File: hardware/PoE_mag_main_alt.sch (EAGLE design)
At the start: 100 parts, among them IC1 LD1117S33TR, IC2 DS1338, IC3 74LVC1T45SOT23-HAND, IC4 ATMEGA1284, IC5 MCP2200, IC6 TSR 1-2450, IC7 74LVC1T45SOT23-HAND, IC8 74LVC1T45SOT23-HAND, IC9 74LVC1T45SOT23-HAND, Q1 2N7002, X1 PWR, X2 JTAG, X3 USB, X4 CONN-SMATHD, X5 UFL, X6 MICRO-SD-SOCKETHIROSE-DM3D, Y1 32k768, Y2 16MHz, Y3 12MHz

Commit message: Layout fixes
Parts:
- added C32: 4u7, SteveMarple:CAP_POLPTH2
- added C33, C34, C35, C36: 100n, SteveMarple:C-EU1206-HAND
- renumbered U$16 to U$2, U$18 to U$3, U$19 to U$4, U$20 to U$5, U$21 to U$6, U$22 to U$7, U$23 to U$8, U$24 to U$9, U$25 to U$10
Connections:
- net +3V3: now also C30.1, C35.1, C36.1; no longer C31.1
- net +5V: no longer C30.1
- net GND: now also C32.-, C33.2, C34.2, C35.2, C36.2
- net VCC: now also C33.1, C34.1
- net V_ANT: now also C31.1, C32.+
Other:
- note added: "74LVC1T45 decoupling"
- note removed: "Battery backup"
- moved on the sheet: C23, C24, C25, C26, C30, C31, JP6

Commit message: Add magnetometer level shifting
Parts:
- added C37, C38: 100n, SteveMarple:C-EU1206-HAND
- added D3: BAS40, SteveMarple:DIODE-SCHOTTKYSOT23-1-3-HAND
- added IC10: PCA9517A, SteveMarple:PCA9517ASOIC
- added JP12: 5V LINK, SparkFun:JUMPER-2PTH
- added JP13: MAG VCC, SparkFun:JUMPER-3PTH
- added R14, R15, R16, R17: 10k, SteveMarple:RESISTOR1206-HAND
- added R18: 3k, SteveMarple:RESISTOR1206-HAND
- added R19: 1k, SteveMarple:RESISTOR1206-HAND
- added X7: RJ45, SteveMarple:RJ45-8PTH
- added X8: RJ11, SteveMarple:RJ11-6PTH
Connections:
- new net MAG_SCL: IC10.SCL_B, R17.1, X7.5, X8.4
- new net MAG_SDA: IC10.SDA_B, R16.1, X7.7, X8.6
- new net MAG_VCC: C37.1, IC10.EN, IC10.VCC_B, JP12.2, R16.2, R17.2, X7.6, X8.5
- new net N$26: JP13.2, X7.8
- net +3V3: now also JP13.3
- net +5V: now also JP12.1
- net 20(SDA): now also IC10.SDA_A, R15.1
- net 21(SCL): now also IC10.SCL_A, R14.1
- net A2: now also D3.A, R18.2, R19.2
- net GND: now also C37.2, C38.2, IC10.GND, R19.1, X7.3, X7.4, X8.2, X8.3
- net VCC: now also C38.1, D3.C, IC10.VCC_A, R14.2, R15.2
- net VIN: now also JP13.1, R18.1, X7.2, X8.1
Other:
- note added: "2.1"
- note added: "SHUTDOWN held low permanently for PoE operation"
- note added: "Voltage selection for battery or power-over-ethernet operation."

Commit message: Add schematics and boards for various modules
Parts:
- added D4: BAS21, SteveMarple:DIODESOT23-1-3-HAND
- added Q2: BSS138, SteveMarple:BSS138SOT23-3-HAND
- added R20: 1M, SteveMarple:RESISTOR1206-HAND
- added R21: 330R, SteveMarple:RESISTOR1206-HAND
- added X9: 22-23-2021, con-molex:22-23-2021
- Q1: value 2N7002 -> BSS138; device SteveMarple:2N7002 -> SteveMarple:BSS138SOT23-3-HAND
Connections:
- new net N$27: D4.C, Q2.D, X9-2.S
- new net N$29: Q2.G, R20.2, R21.2
- net 8: now also R21.1
- net GND: now also D4.A, Q2.S, R20.1
- net VIN: now also X9-1.S
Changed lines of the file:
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@@
 <part name="FRAME1" library="SteveMarple" deviceset="FRAME-A3" device=""/>
 <part name="X3" library="SteveMarple" deviceset="USB" device="PTH" value="USB"/>
-<part name="Q1" library="SteveMarple" deviceset="2N7002" device=""/>
+<part name="Q1" library="SteveMarple" deviceset="BSS138" device="SOT23-3-HAND" value="BSS138"/>
 <part name="IC2" library="SteveMarple" deviceset="DS1307" device="SO08" value="DS1338"/>
 <part name="LED1" library="SparkFun" deviceset="LED" device="3MM" value="D13"/>
@@
 <part name="GND45" library="supply1" deviceset="GND" device=""/>
 <part name="GND46" library="supply1" deviceset="GND" device=""/>
+<part name="R20" library="SteveMarple" deviceset="RESISTOR" device="1206-HAND" value="1M"/>
+<part name="R21" library="SteveMarple" deviceset="RESISTOR" device="1206-HAND" value="330R"/>
+<part name="GND47" library="supply1" deviceset="GND" device=""/>
+<part name="Q2" library="SteveMarple" deviceset="BSS138" device="SOT23-3-HAND" value="BSS138"/>
+<part name="D4" library="SteveMarple" deviceset="DIODE" device="SOT23-1-3-HAND" value="BAS21"/>
+<part name="GND48" library="supply1" deviceset="GND" device=""/>
+<part name="X9" library="con-molex" deviceset="22-23-2021" device=""/>
 </parts>
 <sheets>
@@
 <instances>
 <instance part="FRAME2" gate="G$1" x="0" y="0"/>
+<instance part="R20" gate="G$1" x="88.9" y="172.72" rot="R90"/>
+<instance part="R21" gate="G$1" x="76.2" y="180.34"/>
+<instance part="GND47" gate="1" x="99.06" y="165.1"/>
+<instance part="Q2" gate="G$1" x="99.06" y="182.88"/>
+<instance part="D4" gate="G$1" x="106.68" y="182.88" rot="R90"/>
+<instance part="GND48" gate="1" x="88.9" y="165.1"/>
+<instance part="X9" gate="-1" x="101.6" y="200.66"/>
+<instance part="X9" gate="-2" x="101.6" y="198.12"/>
 </instances>
 <busses>
 </busses>
 <nets>
+<net name="GND" class="1">
+<segment>
+<pinref part="GND47" gate="1" pin="GND"/>
+<wire x1="99.06" y1="167.64" x2="99.06" y2="177.8" width="0.1524" layer="91"/>
+<pinref part="Q2" gate="G$1" pin="S"/>
+<junction x="99.06" y="177.8"/>
+<pinref part="D4" gate="G$1" pin="A"/>
+<wire x1="99.06" y1="177.8" x2="106.68" y2="177.8" width="0.1524" layer="91"/>
+</segment>
+<segment>
+<pinref part="R20" gate="G$1" pin="1"/>
+<pinref part="GND48" gate="1" pin="GND"/>
+</segment>
+</net>
+<net name="N$27" class="0">
+<segment>
+<pinref part="Q2" gate="G$1" pin="D"/>
+<junction x="99.06" y="187.96"/>
+<wire x1="99.06" y1="187.96" x2="99.06" y2="198.12" width="0.1524" layer="91"/>
+<pinref part="D4" gate="G$1" pin="C"/>
+<wire x1="106.68" y1="187.96" x2="99.06" y2="187.96" width="0.1524" layer="91"/>
+<pinref part="X9" gate="-2" pin="S"/>
+</segment>
+</net>
+<net name="N$29" class="0">
+<segment>
+<pinref part="R21" gate="G$1" pin="2"/>
+<pinref part="Q2" gate="G$1" pin="G"/>
+<wire x1="81.28" y1="180.34" x2="88.9" y2="180.34" width="0.1524" layer="91"/>
+<junction x="88.9" y="180.34"/>
+<wire x1="88.9" y1="180.34" x2="93.98" y2="180.34" width="0.1524" layer="91"/>
+<pinref part="R20" gate="G$1" pin="2"/>
+<wire x1="88.9" y1="180.34" x2="88.9" y2="177.8" width="0.1524" layer="91"/>
+</segment>
+</net>
+<net name="8" class="0">
+<segment>
+<pinref part="R21" gate="G$1" pin="1"/>
+<wire x1="71.12" y1="180.34" x2="68.58" y2="180.34" width="0.1524" layer="91"/>
+<label x="66.04" y="180.34" size="1.778" layer="95" rot="MR0"/>
+</segment>
+</net>
+<net name="VIN" class="1">
+<segment>
+<pinref part="X9" gate="-1" pin="S"/>
+<wire x1="99.06" y1="200.66" x2="99.06" y2="208.28" width="0.1524" layer="91"/>
+<label x="99.06" y="210.82" size="1.778" layer="95" rot="R90"/>
+</segment>
+</net>
 </nets>
 </sheet>
@@
 <instance part="FRAME1" gate="G$1" x="-172.72" y="-76.2"/>
 <instance part="X3" gate="G$1" x="-144.78" y="-20.32" smashed="yes" rot="MR0"/>
-<instance part="Q1" gate="A" x="185.42" y="132.08"/>
+<instance part="Q1" gate="G$1" x="185.42" y="132.08"/>
 <instance part="IC2" gate="G$1" x="142.24" y="66.04"/>
 <instance part="LED1" gate="G$1" x="185.42" y="142.24"/>
@@
 </segment>
 <segment>
-<pinref part="Q1" gate="A" pin="S"/>
+<pinref part="Q1" gate="G$1" pin="S"/>
 <pinref part="GND3" gate="1" pin="GND"/>
 <wire x1="185.42" y1="127" x2="185.42" y2="119.38" width="0.1524" layer="91"/>
@@
 <segment>
 <pinref part="LED1" gate="G$1" pin="C"/>
-<pinref part="Q1" gate="A" pin="D"/>
+<pinref part="Q1" gate="G$1" pin="D"/>
 </segment>
 </net>
@@
 </segment>
 <segment>
-<pinref part="Q1" gate="A" pin="G"/>
+<pinref part="Q1" gate="G$1" pin="G"/>
 <wire x1="180.34" y1="129.54" x2="172.72" y2="129.54" width="0.1524" layer="91"/>
 <label x="165.1" y="129.54" size="1.778" layer="95" rot="MR0"/>

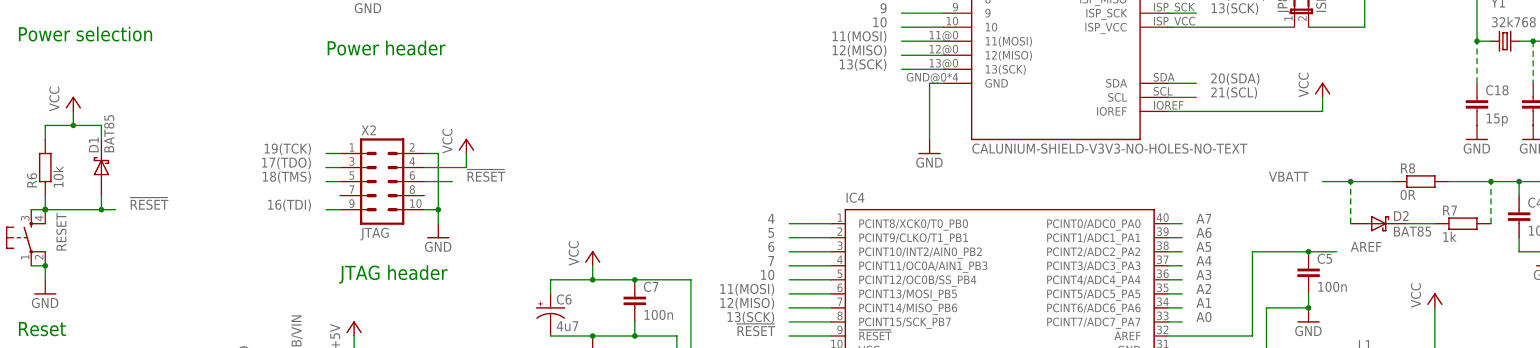
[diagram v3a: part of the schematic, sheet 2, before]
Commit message: Add Fibox box outline
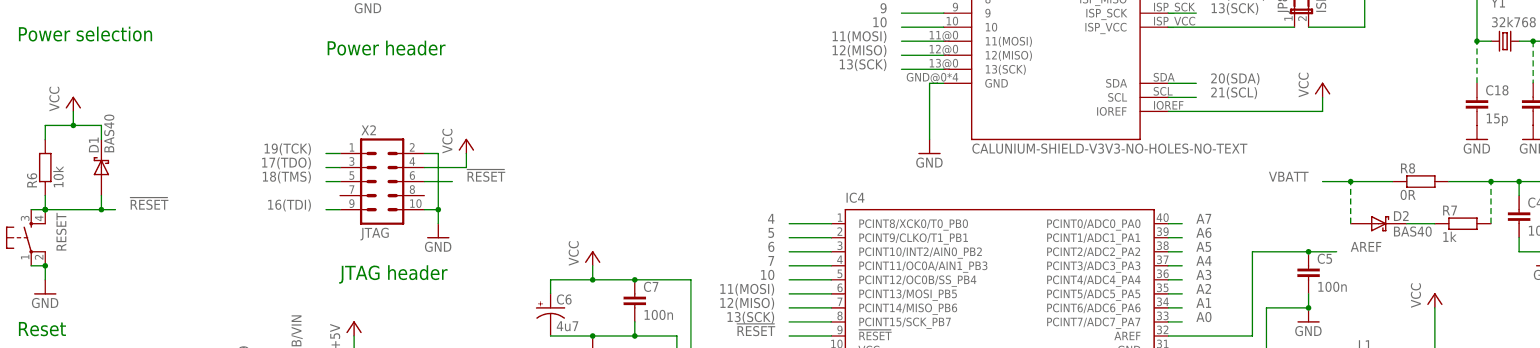
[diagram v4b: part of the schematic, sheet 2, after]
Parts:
- D1, D2: value BAT85 -> BAS40
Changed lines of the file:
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@@
 </part>
 <part name="GND6" library="supply1" deviceset="GND" device=""/>
-<part name="D1" library="SteveMarple" deviceset="DIODE-SCHOTTKY" device="SOT23-1-3-HAND" value="BAT85"/>
-<part name="D2" library="SteveMarple" deviceset="DIODE-SCHOTTKY" device="SOT23-1-3-HAND" value="BAT85"/>
+<part name="D1" library="SteveMarple" deviceset="DIODE-SCHOTTKY" device="SOT23-1-3-HAND" value="BAS40"/>
+<part name="D2" library="SteveMarple" deviceset="DIODE-SCHOTTKY" device="SOT23-1-3-HAND" value="BAS40"/>
 <part name="C4" library="SteveMarple" deviceset="C-EU" device="1206-HAND" value="100p"/>
 <part name="R7" library="SteveMarple" deviceset="RESISTOR" device="1206-HAND" value="1k"/>

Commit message: Updates
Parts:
- removed Q2: BSS138, SteveMarple:BSS138SOT23-3-HAND
- added BOX1: BOXFIBOX-PC-M-95-G, fibox:BOXFIBOX-PC-M-95-G
- added Q3: BUK98150-55A, SteveMarple:FET-N-TYPESOT223-HAND
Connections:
- net GND: now also Q3.S; no longer Q2.S
- net N$27: now also Q3.D; no longer Q2.D
- net N$29: now also Q3.G; no longer Q2.G
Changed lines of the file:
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@@
 <part name="R21" library="SteveMarple" deviceset="RESISTOR" device="1206-HAND" value="330R"/>
 <part name="GND47" library="supply1" deviceset="GND" device=""/>
-<part name="Q2" library="SteveMarple" deviceset="BSS138" device="SOT23-3-HAND" value="BSS138"/>
 <part name="D4" library="SteveMarple" deviceset="DIODE" device="SOT23-1-3-HAND" value="BAS21"/>
 <part name="GND48" library="supply1" deviceset="GND" device=""/>
 <part name="X9" library="con-molex" deviceset="22-23-2021" device=""/>
+<part name="BOX1" library="fibox" deviceset="BOX" device="FIBOX-PC-M-95-G"/>
+<part name="Q3" library="SteveMarple" deviceset="FET-N-TYPE" device="SOT223-HAND" value="BUK98150-55A"/>
 </parts>
 <sheets>
@@
 <instance part="R21" gate="G$1" x="76.2" y="180.34"/>
 <instance part="GND47" gate="1" x="99.06" y="165.1"/>
-<instance part="Q2" gate="G$1" x="99.06" y="182.88"/>
 <instance part="D4" gate="G$1" x="106.68" y="182.88" rot="R90"/>
 <instance part="GND48" gate="1" x="88.9" y="165.1"/>
 <instance part="X9" gate="-1" x="101.6" y="200.66"/>
 <instance part="X9" gate="-2" x="101.6" y="198.12"/>
+<instance part="BOX1" gate="G$1" x="342.9" y="50.8"/>
+<instance part="Q3" gate="G$1" x="99.06" y="182.88"/>
 </instances>
 <busses>
@@
 <pinref part="GND47" gate="1" pin="GND"/>
 <wire x1="99.06" y1="167.64" x2="99.06" y2="177.8" width="0.1524" layer="91"/>
-<pinref part="Q2" gate="G$1" pin="S"/>
 <junction x="99.06" y="177.8"/>
 <pinref part="D4" gate="G$1" pin="A"/>
 <wire x1="99.06" y1="177.8" x2="106.68" y2="177.8" width="0.1524" layer="91"/>
+<pinref part="Q3" gate="G$1" pin="S"/>
 </segment>
 <segment>
@@
 <net name="N$27" class="0">
 <segment>
-<pinref part="Q2" gate="G$1" pin="D"/>
 <junction x="99.06" y="187.96"/>
 <wire x1="99.06" y1="187.96" x2="99.06" y2="198.12" width="0.1524" layer="91"/>
@@
 <wire x1="106.68" y1="187.96" x2="99.06" y2="187.96" width="0.1524" layer="91"/>
 <pinref part="X9" gate="-2" pin="S"/>
+<pinref part="Q3" gate="G$1" pin="D"/>
 </segment>
 </net>
@@
 <segment>
 <pinref part="R21" gate="G$1" pin="2"/>
-<pinref part="Q2" gate="G$1" pin="G"/>
 <wire x1="81.28" y1="180.34" x2="88.9" y2="180.34" width="0.1524" layer="91"/>
 <junction x="88.9" y="180.34"/>
@@
 <pinref part="R20" gate="G$1" pin="2"/>
 <wire x1="88.9" y1="180.34" x2="88.9" y2="177.8" width="0.1524" layer="91"/>
+<pinref part="Q3" gate="G$1" pin="G"/>
 </segment>
 </net>

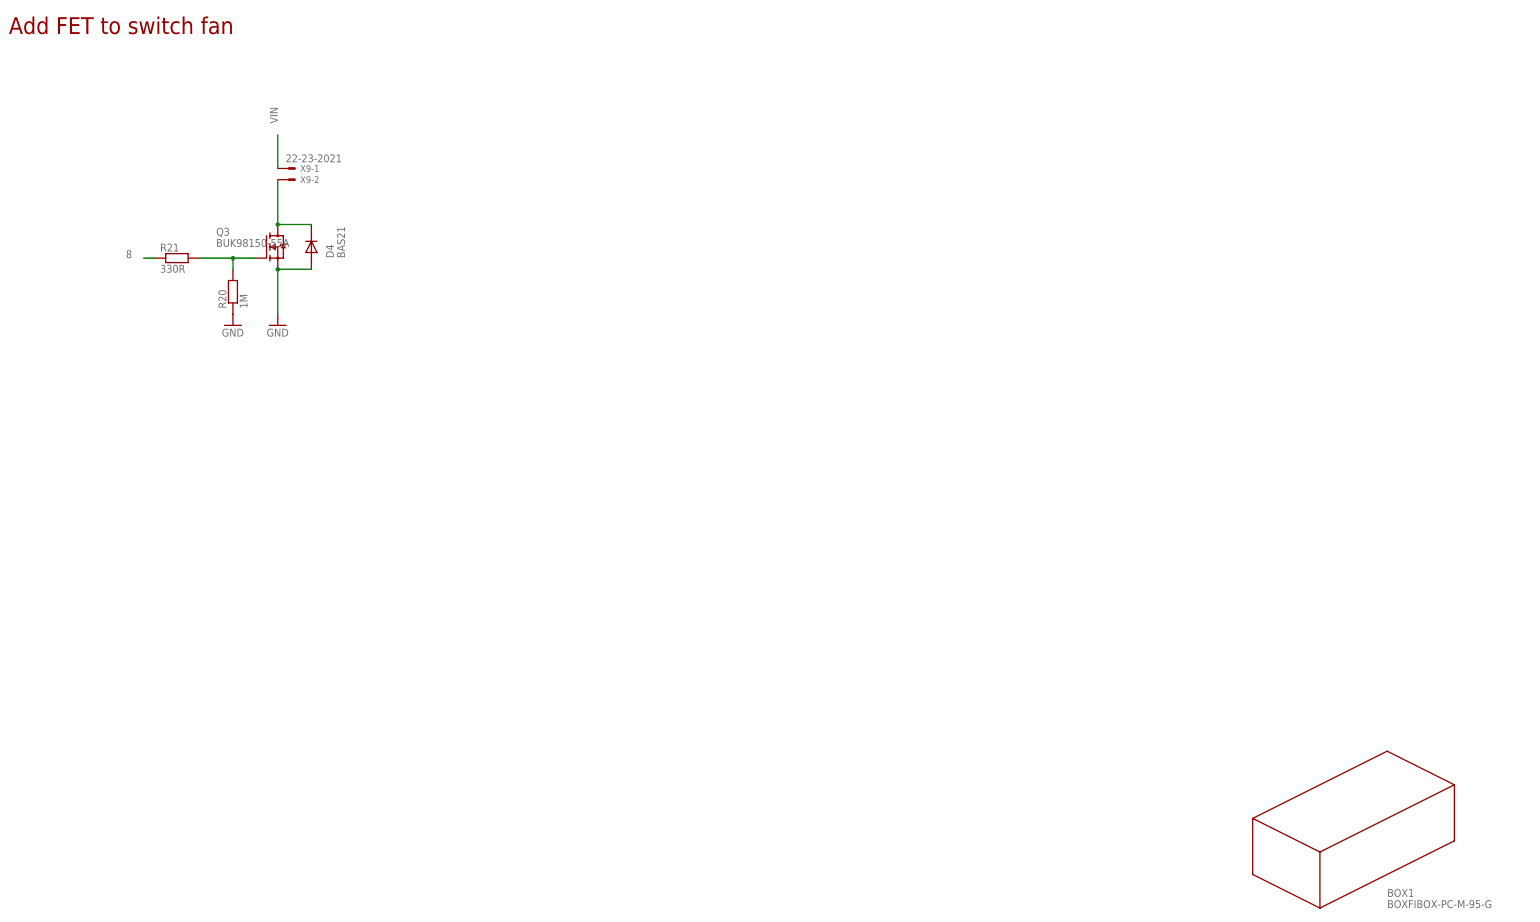
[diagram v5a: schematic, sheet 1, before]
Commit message: Update enclosure outline, move components
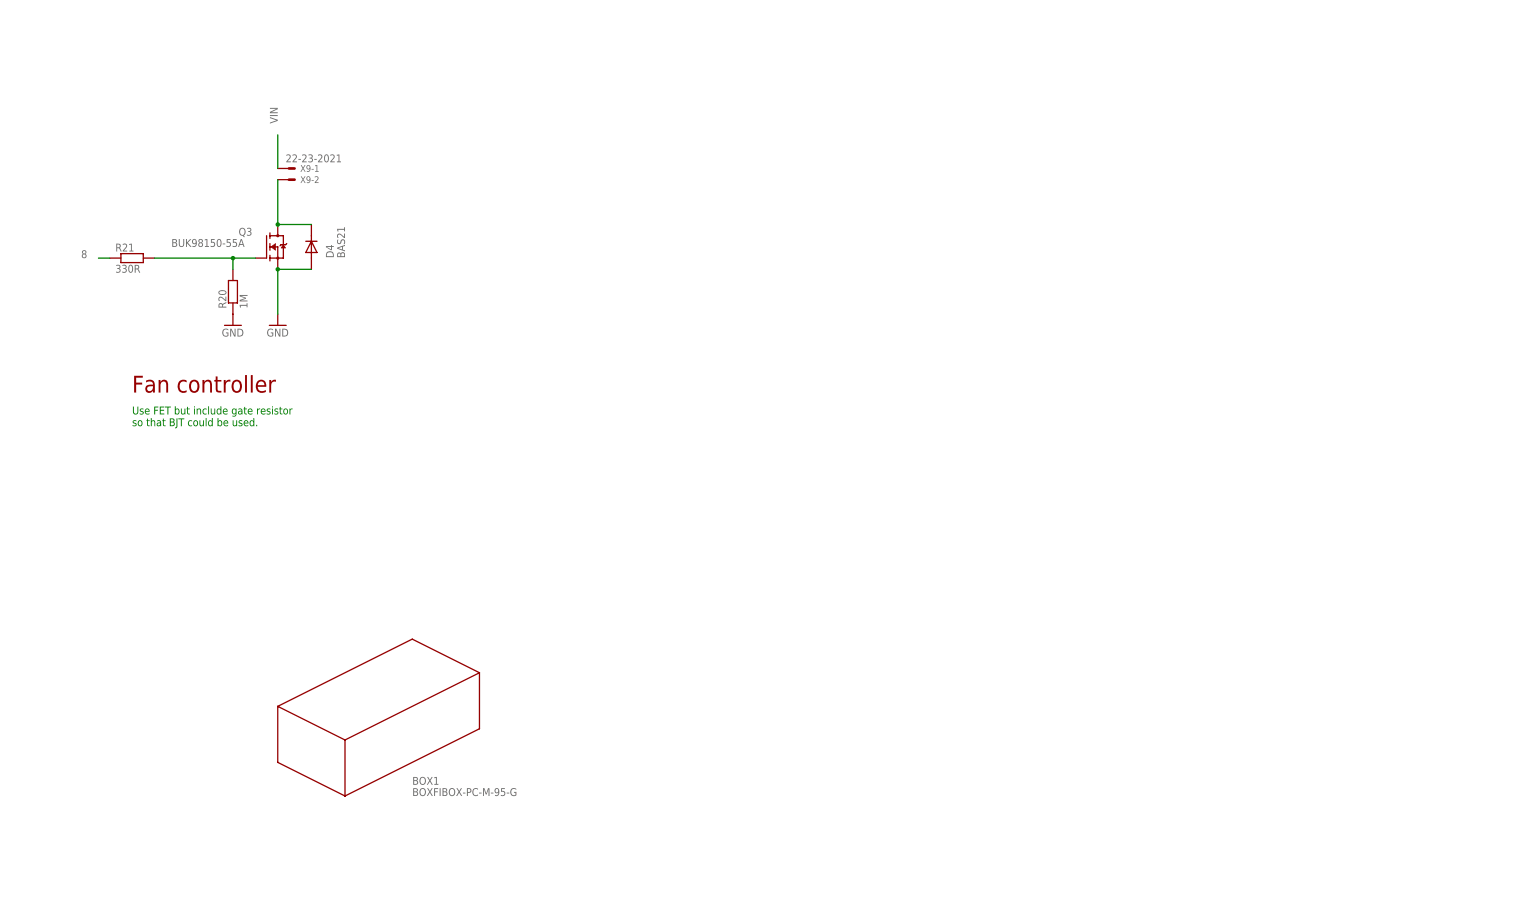
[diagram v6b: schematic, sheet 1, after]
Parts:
- removed H1, H2, H3, H4: MOUNT-PAD-ROUND3.0, holes:MOUNT-PAD-ROUND3.0
- R18: value 3k -> 3k 1%
- R19: value 1k -> 1k 1%
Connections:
- net GND: no longer H1.MOUNT, H2.MOUNT, H3.MOUNT, H4.MOUNT
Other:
- note added: "Fan controller"
- note added: "Use FET but include gate resistor so that BJT could be used."
- note removed: "Add FET to switch fan"
- moved on the sheet: BOX1, R21
